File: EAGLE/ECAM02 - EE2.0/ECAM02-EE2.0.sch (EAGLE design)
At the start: 61 parts, among them J1 MODULAR TOOL, J2 SPI, J3 MOT, J4 FTDI, J5 S4B-PH-SM4, J6 SOL+PUMP, J7 RINGLIGHT, Q2 16MHz, U1 SP3485, U10 MCP4725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

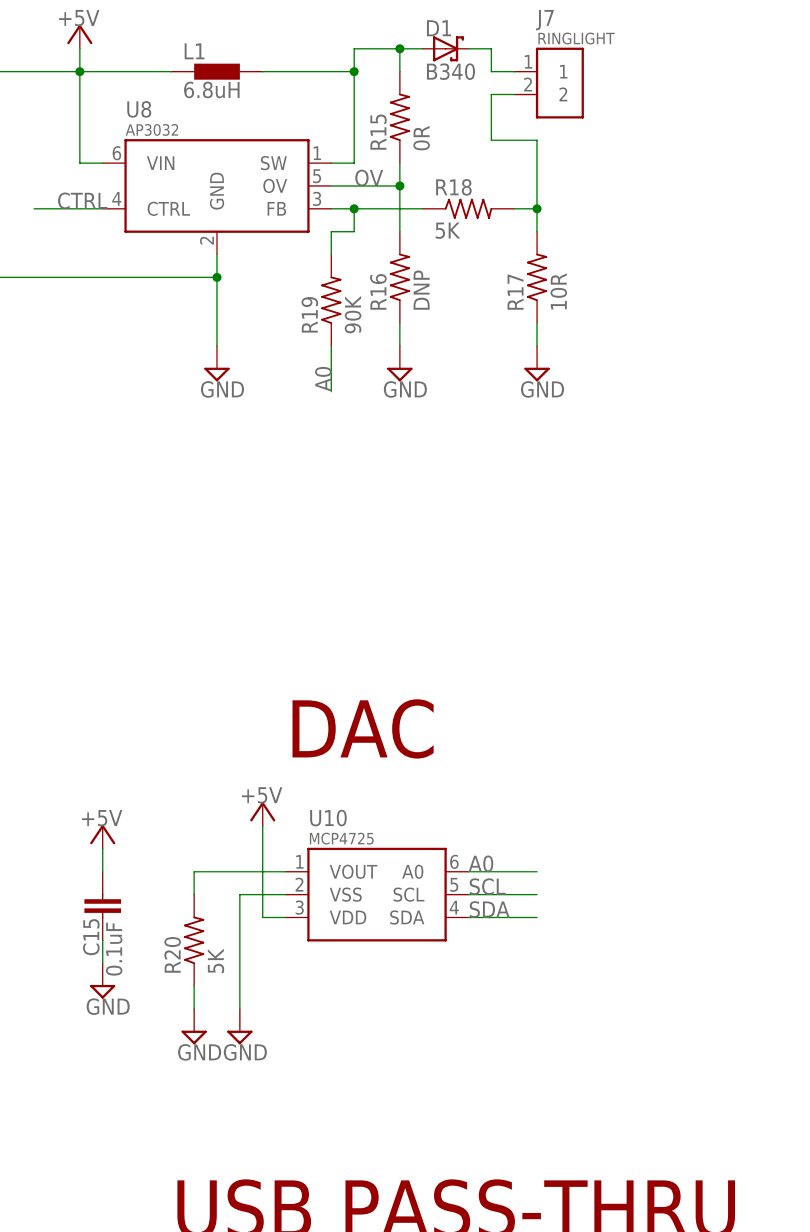
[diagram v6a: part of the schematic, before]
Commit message: Re-jiggered switching power supply for LED controller.  Re-routed and whatnot.  Generated GERBERs for REV--
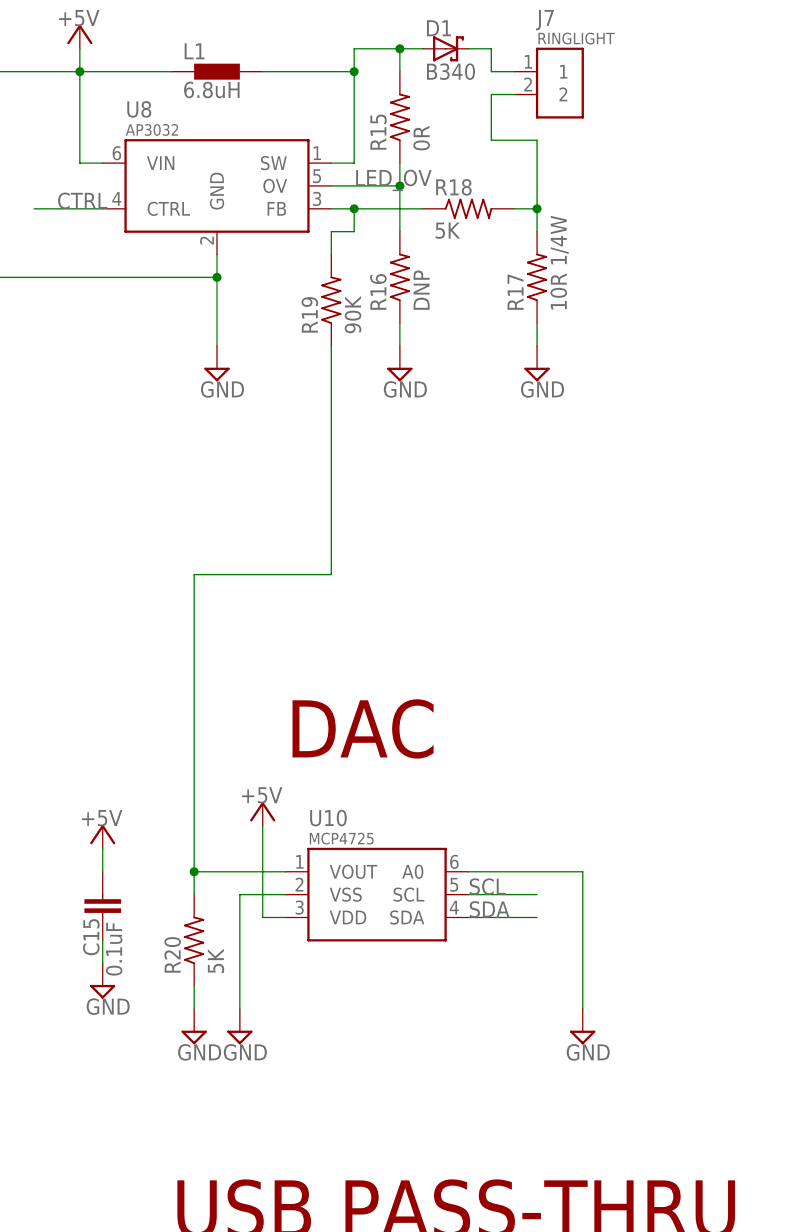
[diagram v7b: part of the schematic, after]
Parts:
- R17: value 10R -> 10R 1/4W; device TinWhiskers:CPL-RES-0603-10.0-0.1W -> TinWhiskers:CPL-RES-1206-10-0.25W1206
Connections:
- net N$1 renamed LED_ANODE
- net N$2 renamed LED_SW
- net N$3 renamed LED_CATHODE
- net N$4 renamed LED_FB
- net OV renamed LED_OV
- removed net A0: R19.1, U10.A0
- net GND: now also U10.A0
- net N$10: now also R19.1
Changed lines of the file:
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@@
 <?xml version="1.0" encoding="utf-8"?>
 <!DOCTYPE eagle SYSTEM "eagle.dtd">
-<eagle version="7.4.0">
+<eagle version="7.3.0">
 <drawing>
 <settings>
@@
 <part name="SUPPLY28" library="TinWhiskers" deviceset="GND" device=""/>
 <part name="+3V4" library="supply1" deviceset="+3V3" device=""/>
-<part name="R17" library="TinWhiskers" deviceset="CPL-RES-0603-10.0-0.1W" device="" value="10R"/>
+<part name="R17" library="TinWhiskers" deviceset="CPL-RES-1206-10-0.25W" device="1206" value="10R 1/4W"/>
 <part name="R18" library="TinWhiskers" deviceset="CPL-RES-0603-5K-0.1W" device="" value="5K"/>
 <part name="R19" library="TinWhiskers" deviceset="CPL-RES-0603-90K-0.1W" device="" value="90K"/>
@@
 <part name="P+17" library="supply1" deviceset="+5V" device=""/>
 <part name="SUPPLY36" library="TinWhiskers" deviceset="GND" device=""/>
+<part name="SUPPLY37" library="TinWhiskers" deviceset="GND" device=""/>
 </parts>
 <sheets>
@@
 </instance>
 <instance part="SUPPLY36" gate="GND" x="256.54" y="180.34"/>
+<instance part="SUPPLY37" gate="GND" x="172.72" y="124.46" smashed="yes">
+<attribute name="VALUE" x="170.815" y="121.285" size="1.778" layer="96"/>
+</instance>
 </instances>
 <busses>
@@
 <wire x1="256.54" y1="187.96" x2="256.54" y2="182.88" width="0.1524" layer="91"/>
 </segment>
+<segment>
+<pinref part="U10" gate="G$1" pin="A0"/>
+<pinref part="SUPPLY37" gate="GND" pin="GND"/>
+<wire x1="160.02" y1="142.24" x2="172.72" y2="142.24" width="0.1524" layer="91"/>
+<wire x1="172.72" y1="142.24" x2="172.72" y2="127" width="0.1524" layer="91"/>
+</segment>
 </net>
 <net name="+24V" class="0">
@@
 </segment>
 </net>
-<net name="N$2" class="0">
+<net name="LED_SW" class="0">
 <segment>
 <pinref part="L1" gate="G$1" pin="2"/>
@@
 </segment>
 </net>
-<net name="OV" class="0">
+<net name="LED_OV" class="0">
 <segment>
 <pinref part="R16" gate="R$1" pin="2"/>
@@
 </segment>
 </net>
-<net name="N$1" class="0">
+<net name="LED_ANODE" class="0">
 <segment>
 <pinref part="D1" gate="G$1" pin="C"/>
@@
 </segment>
 </net>
-<net name="N$3" class="0">
+<net name="LED_CATHODE" class="0">
 <segment>
 <pinref part="J7" gate="G$1" pin="2"/>
@@
 </segment>
 </net>
-<net name="N$4" class="0">
+<net name="LED_FB" class="0">
 <segment>
 <pinref part="U8" gate="G$1" pin="FB"/>
@@
 <pinref part="R20" gate="G$1" pin="2"/>
 <wire x1="129.54" y1="139.7" x2="129.54" y2="142.24" width="0.1524" layer="91"/>
-</segment>
-</net>
-<net name="A0" class="0">
-<segment>
-<pinref part="U10" gate="G$1" pin="A0"/>
-<wire x1="160.02" y1="142.24" x2="167.64" y2="142.24" width="0.1524" layer="91"/>
-<label x="160.02" y="142.24" size="1.778" layer="95"/>
-</segment>
-<segment>
 <pinref part="R19" gate="G$1" pin="1"/>
-<wire x1="144.78" y1="200.66" x2="144.78" y2="195.58" width="0.1524" layer="91"/>
-<label x="144.78" y="195.58" size="1.778" layer="95" ratio="10" rot="R90"/>
-</segment>
-</net>
+<wire x1="144.78" y1="200.66" x2="144.78" y2="175.26" width="0.1524" layer="91"/>
+<wire x1="144.78" y1="175.26" x2="129.54" y2="175.26" width="0.1524" layer="91"/>
+<wire x1="129.54" y1="175.26" x2="129.54" y2="142.24" width="0.1524" layer="91"/>
+<junction x="129.54" y="142.24"/>
+</segment>
+</net>

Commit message: BOMs complete for all FPD boards
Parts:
- C12: PARTNO (none) -> GRM188R61C106MA73D
- C13, C14, C15, C16: PARTNO (none) -> GMK107BJ104KAHT
- C17: PARTNO (none) -> EMVA500ADA101MHA0G
- C18: PARTNO (none) -> EMVH350ADA100MF60G
- D1: PARTNO (none) -> B340A-13-F
- J1: PARTNO S8B-PH-SM4-TB(LF)(SN) -> B8B-PH-SM4-TB(LF)(SN)
- J2: PARTNO (none) -> 67996-206HLF
- J6: PARTNO (none) -> B7B-PH-SM4-TB(LF)(SN)
- J7: PARTNO (none) -> B2B-PH-SM4-TB(LF)(SN)
- L1: PARTNO (none) -> BRL1608T6R8M
- R15, R16: PARTNO (none) -> RC0603JR-070RL
- R17: PARTNO (none) -> RC1206FR-0710RL
- R18, R20: PARTNO (none) -> PNM0603E5001BST5
- R19: PARTNO (none) -> RC0603FR-0790K9L
- U10: PARTNO (none) -> MCP4725A0T-E/CH
- U11, U4, U5, U6, U7: PARTNO (none) -> NTR4003NT3G
- U8: PARTNO (none) -> AP3032KTR-G1
- U9: PARTNO (none) -> SN74LVC1G32DBVR
